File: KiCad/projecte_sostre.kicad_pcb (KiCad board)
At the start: 2 copper layers, 97.6 x 92.1 mm, 149 parts, among them J1 Conn_01x02, J10 DE9_Pins, J11 DE9_Pins, J2 Conn_01x05, J3 Conn_01x02, J4 Conn_01x02, J5 Conn_01x02, J6 Conn_01x02, J7 Screw_Terminal_01x02, J8 Screw_Terminal_01x02, J9 Screw_Terminal_01x02, SW1 SW_Push, SW2 SW_Push, SW3 SW_Push, SW4 SW_Push, SW5 SW_Push, SW6 SW_Push, U1 74AHCT1G125, U10 MCP2561-E-MF, U11 MAX3232, U12 A1101xLH, U13 A1101xLH, U14 L298P, U2 LM393, U3 LM393, U4 PIC24HJ128GP502, U5 LM1117DT-3.3, U6 LM2596T-5, U8 INA219AxD, U9 INA219AxD, Y1 Crystal

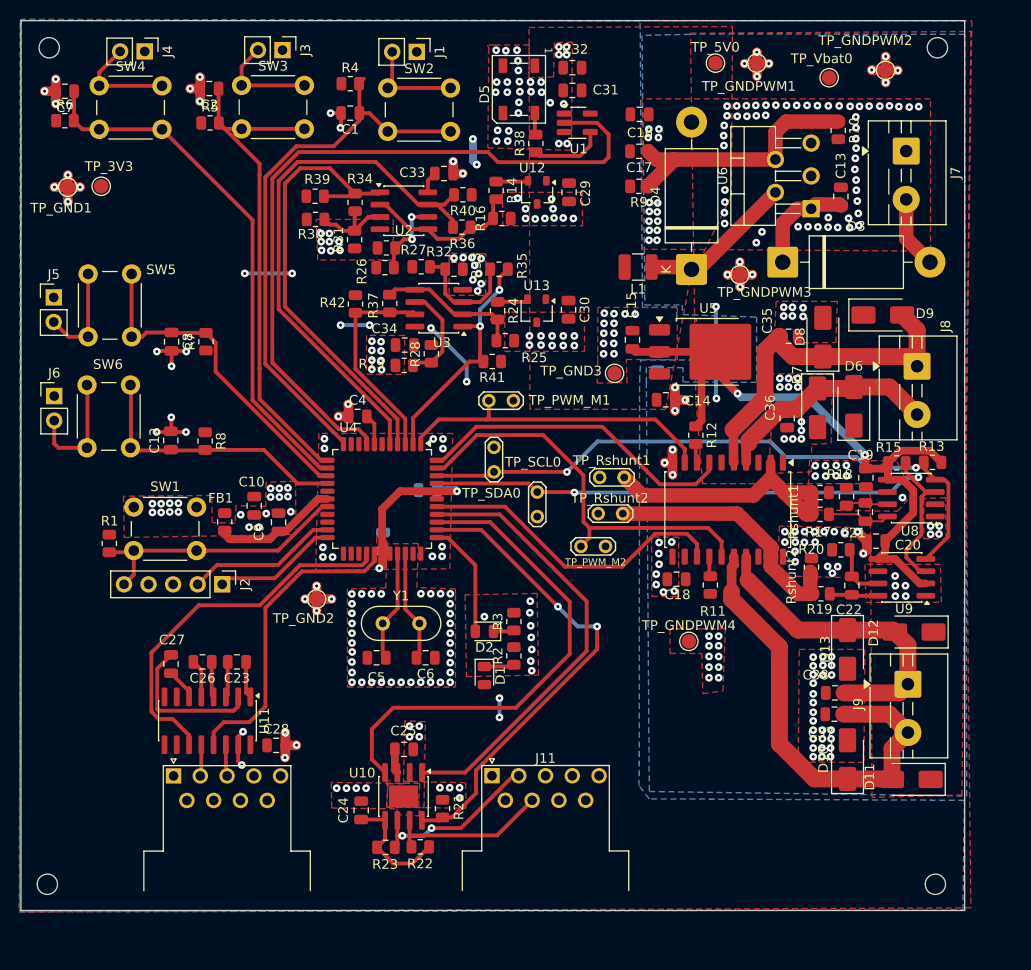
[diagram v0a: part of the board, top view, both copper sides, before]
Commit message: PCB casi acabada, despues de revisión de ayer 27/04 y cambio en componente CAN, que se vera reflejado en README y en DB
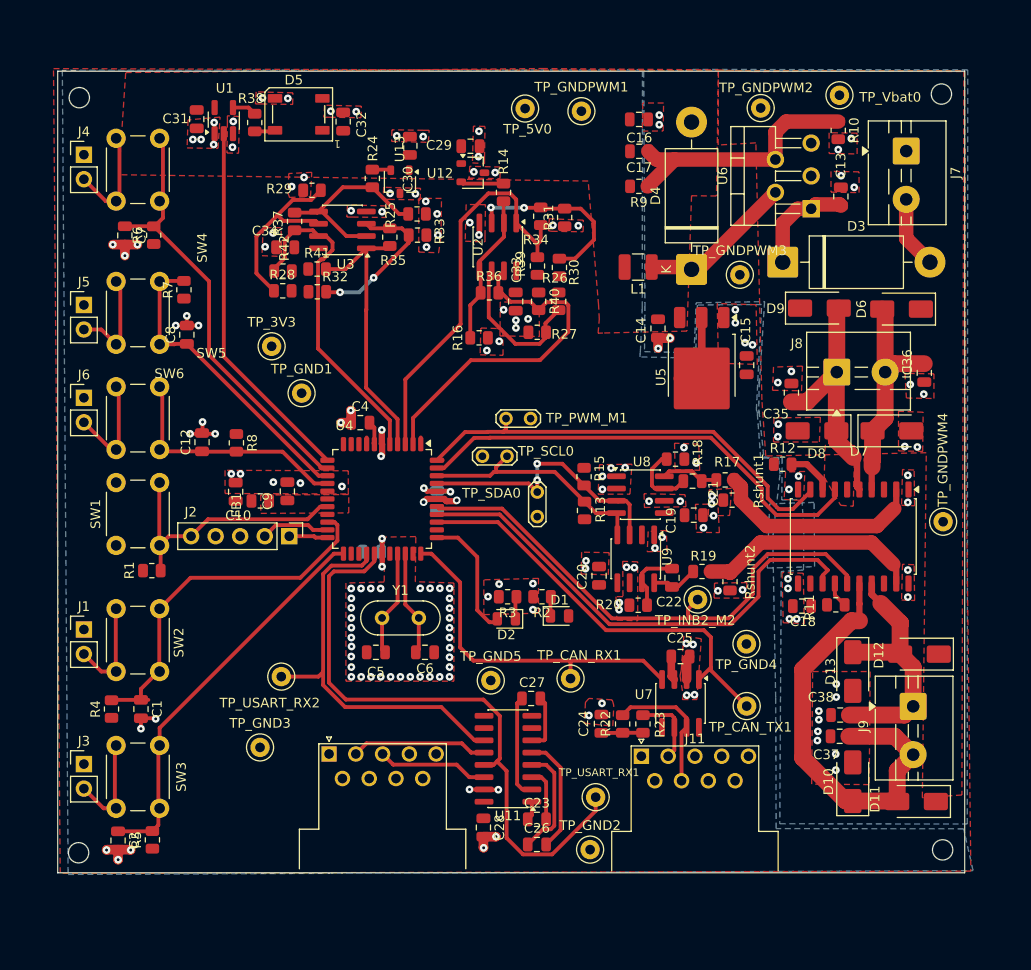
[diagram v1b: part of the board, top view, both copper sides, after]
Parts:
- removed R21: 10k, Resistor_SMD:R_0805_2012Metric
- removed R43: 0, Resistor_SMD:R_0805_2012Metric
- removed TP_PWM_M2, TP_Rshunt1, TP_Rshunt2: TestPoint_2Pole, TestPoint:TestPoint_2Pads_Pitch2.54mm_Drill0.8mm
- removed U10: MCP2561-E-MF, Package_SO:SOIC-8-1EP_3.9x4.9mm_P1.27mm_EP2.29x3mm
- added TP_CAN_RX1: TestPoint, TestPoint:TestPoint_Keystone_5000-5004_Miniature, F.Cu at (157.4, 123.7)
- added TP_CAN_TX1: TestPoint, TestPoint:TestPoint_Keystone_5000-5004_Miniature, F.Cu at (175.7, 126.5)
- added TP_GND4: TestPoint, TestPoint:TestPoint_Keystone_5000-5004_Miniature, F.Cu at (175.7, 120.1)
- added TP_GND5: TestPoint, TestPoint:TestPoint_Keystone_5000-5004_Miniature, F.Cu at (149.2, 123.9)
- added TP_INB2_M2: TestPoint, TestPoint:TestPoint_Keystone_5000-5004_Miniature, F.Cu at (170.6, 115.5)
- added TP_USART_RX1: TestPoint, TestPoint:TestPoint_Keystone_5000-5004_Miniature, F.Cu at (160.1, 135.9)
- added TP_USART_RX2: TestPoint, TestPoint:TestPoint_Keystone_5000-5004_Miniature, F.Cu at (127.5, 123.5)
- added U7: SN65HVD232, Package_SO:SOIC-8_3.9x4.9mm_P1.27mm, F.Cu at (168.8, 126.2)
- TP_3V3, TP_5V0, TP_GND1, TP_GND2, TP_GND3, TP_GNDPWM1, TP_GNDPWM2, TP_GNDPWM3, TP_GNDPWM4, TP_Vbat0: footprint TestPoint:TestPoint_Pad_D1.5mm -> TestPoint:TestPoint_Keystone_5000-5004_Miniature
- moved C2 78.4 mm to (110.6, 140.4), turned to -90 degrees
- moved J3 76.7 mm to (107.1, 132.5), turned to 0 degrees
- moved SW3 75.9 mm to (110.4, 137.1), turned to 90 degrees
- moved R5 74.4 mm to (114.2, 140.4), turned to 90 degrees
- moved R4 69.3 mm to (110.0, 126.8), turned to 90 degrees
- moved J1 69.0 mm to (107.1, 118.6), turned to 0 degrees
- moved SW2 66.6 mm to (110.4, 123.0), turned to 90 degrees
- moved C1 65.3 mm to (113.0, 126.8), turned to -90 degrees
- moved TP_GND3 53.3 mm to (125.3, 130.8)
- moved C26 39.4 mm to (154.0, 140.8), turned to 0 degrees
- moved C31 39.0 mm to (118.8, 65.8), turned to -90 degrees
- moved TP_GND2 38.4 mm to (159.5, 141.4)
- moved C27 37.4 mm to (153.4, 125.7), turned to 0 degrees
- moved U1 36.6 mm to (121.6, 66.0), turned to 90 degrees
- moved R13 36.4 mm to (158.9, 106.3), turned to 90 degrees
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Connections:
- net /Digital/SPLIT renamed /Digital/entre_R_par_diferencial_y_C
- C21 pad 1: /Analogica/IN+ -> /Analogica/IN+_M1
- C21 pad 2: /Analogica/IN- -> /Analogica/IN-_M1
- C22 pad 1: /Analogica/IN+ -> /Analogica/IN+_M2
- C22 pad 2: /Analogica/IN- -> /Analogica/IN-_M2
- R17 pad 1: /Analogica/IN+ -> /Analogica/IN+_M1
- R18 pad 2: /Analogica/IN- -> /Analogica/IN-_M1
- R19 pad 1: /Analogica/IN+ -> /Analogica/IN+_M2
- R20 pad 2: /Analogica/IN- -> /Analogica/IN-_M2
- U4 pad 1: INA2_M1 -> unconnected-(U4-RB9-Pad1)
- U4 pad 11: M1_go_Max -> unconnected-(U4-RB13-Pad11)
- U4 pad 12: M1_go_Min -> LED_RGB
- U4 pad 2: DOWN_LOW_M1_Pos_Min -> HIGH_UP_M1_Pos_Max
- U4 pad 20: unconnected-(U4-AN1/C12IN1-/CTCMP/RA1-Pad20) -> M1_go_Max
- U4 pad 23: unconnected-(U4-RB2-Pad23) -> M1_go_Min
- U4 pad 3: HIGH_UP_M1_Pos_Min -> DOWN_LOW_M1_Pos_Max
- U4 pad 33: unconnected-(U4-RB4-Pad33) -> CAN_RX
- U4 pad 35: STBY_Trans_CAN -> unconnected-(U4-RA9-Pad35)
- U4 pad 36: CAN_RX -> CAN_TX
- U4 pad 37: CAN_TX -> INB1_M2
- U4 pad 38: INB1_M2 -> INB2_M2
- U4 pad 4: DOWN_LOW_M1_Pos_Max -> DOWN_LOW_M1_Pos_Min
- U4 pad 43: INB2_M2 -> INA1_M1
- U4 pad 44: INA1_M1 -> INA2_M1
- U4 pad 5: HIGH_UP_M1_Pos_Max -> HIGH_UP_M1_Pos_Min
- U4 pad 8: LED_RGB -> unconnected-(U4-PGED2/RB10-Pad8)
- U8 pad 7: /Analogica/IN- -> /Analogica/IN-_M1
- U8 pad 8: /Analogica/IN+ -> /Analogica/IN+_M1
- U9 pad 7: /Analogica/IN- -> /Analogica/IN-_M2
- U9 pad 8: /Analogica/IN+ -> /Analogica/IN+_M2
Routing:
- net +3.3V: track 115.0 -> 25.8 mm, vias 14 -> 4
- net STBY_Trans_CAN: track 49.9 -> 0.00 mm, vias 2 -> 0
- net I2C_SCL: track 66.0 -> 24.9 mm, vias 2 -> 0
- net I2C_SDA: track 67.2 -> 28.2 mm
- net LED_RGB: track 76.8 -> 38.2 mm
- net USART_RX: track 32.0 -> 64.1 mm
- net GND: track 67.9 -> 36.1 mm, vias 384 -> 172
- net HIGH_UP_M1_Pos_Max: track 57.2 -> 36.2 mm
- net M1_go_Max: track 57.9 -> 38.1 mm
- net INB1_M2: track 32.7 -> 51.5 mm
- net CAN_RX: track 51.3 -> 36.2 mm
- net INA1_M1: track 33.5 -> 48.1 mm
- net INB2_M2: track 42.1 -> 55.8 mm
- net INA2_M1: track 33.5 -> 47.0 mm
- net /Microprocesador/AVDD: track 12.9 -> 0.00 mm
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- added copper zone on F.Cu, net /Microprocesador/AVDD
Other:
- board size 97.6 x 92.1 mm -> 93.8 x 82.9 mm

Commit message: Layout definitivo
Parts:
- removed C33: 100n, Capacitor_SMD:C_0805_2012Metric
- removed R24, R26, R28, R31, R33, R39, R40, R41, R42: 10k, Resistor_SMD:R_0805_2012Metric
- removed R25: 20k, Resistor_SMD:R_0805_2012Metric
- removed R27, R29, R30, R32: 22k, Resistor_SMD:R_0805_2012Metric
- removed R34, R35, R36, R37: 220k, Resistor_SMD:R_0805_2012Metric
- removed TP_PWM_M1, TP_SCL0, TP_SDA0: TestPoint_2Pole, TestPoint:TestPoint_2Pads_Pitch2.54mm_Drill0.8mm
- removed U2: LM393, Package_SO:SOIC-8_3.9x4.9mm_P1.27mm
- added GND10: TestPoint, TestPoint:TestPoint_Keystone_5000-5004_Miniature, F.Cu at (158.4, 95.2)
- added PWM_M1: TestPoint, TestPoint:TestPoint_Keystone_5000-5004_Miniature, F.Cu at (153.0, 97.3)
- added SCL0: TestPoint, TestPoint:TestPoint_Keystone_5000-5004_Miniature, F.Cu at (149.9, 100.7)
- added SDA0: TestPoint, TestPoint:TestPoint_Keystone_5000-5004_Miniature, F.Cu at (153.9, 104.5)
- R16: value 20k -> 10k
- moved RX2 25.0 mm to (137.2, 125.8)
- moved C34 24.3 mm to (150.4, 88.3), turned to 0 degrees
- moved TP_3V3 15.7 mm to (123.0, 74.0)
- moved GND1 15.6 mm to (123.0, 80.0)
- moved U3 14.6 mm to (145.9, 85.6), turned to -90 degrees
- moved TX2 13.8 mm to (140.6, 128.0)
- moved U13 13.7 mm to (151.9, 78.8), turned to 0 degrees
- moved R14 13.1 mm to (140.6, 81.9), turned to 0 degrees
- moved C30 13.0 mm to (151.6, 75.8), turned to 0 degrees
- moved C26 9.29 mm to (156.7, 131.9), turned to 90 degrees
- moved U12 8.84 mm to (142.6, 78.8)
- moved C29 8.63 mm to (142.5, 75.9)
- moved R16 8.20 mm to (153.1, 82.0)
- moved C15 7.68 mm to (169.6, 95.9), turned to 0 degrees
- moved C14 6.89 mm to (173.3, 86.7), turned to 180 degrees
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- renumbered TP_GND1 to GND1, TP_GNDPWM1 to GND2, TP_GNDPWM2 to GND3, TP_GND5 to GND4, TP_GND2 to GND5, TP_GND3 to GND6, TP_GNDPWM3 to GND7, TP_GNDPWM4 to GND8, TP_GND4 to GND9, TP_INB2_M2 to PWM_M2, TP_CAN_RX1 to RX1, TP_USART_RX1 to RX2, Rshunt1 to Rsht1, Rshunt2 to Rsht2, TP_CAN_TX1 to TX1, TP_USART_RX2 to TX2
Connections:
- J1 pad 2: /Microprocesador/Conn_SW_M1_Max -> M1_go_Max
- J3 pad 2: /Microprocesador/Conn_SW_M1_Min -> M1_go_Min
- J4 pad 2: /Microprocesador/Conn_SW_M2_Max -> M2_go_Max
- J5 pad 2: /Microprocesador/Conn_SW_M2_Min -> M2_go_Min
- J6 pad 2: /Microprocesador/Conn_SW_LED_ON/OFF -> ON/OFF_LED
- R14 pad 1: /Digital/SHall1_entre_Vout_y_Rdivisor -> +3.3V
- R14 pad 2: /Digital/VOUT_Hall1 -> /Digital/entre_sHall_R14
- R16 pad 1: GND -> +3.3V
- R16 pad 2: /Digital/VOUT_Hall1 -> /Digital/entre_sHall_R16
- SW2 pad 1: /Microprocesador/Conn_SW_M1_Max -> GND
- SW3 pad 1: /Microprocesador/Conn_SW_M1_Min -> GND
- SW4 pad 1: /Microprocesador/Conn_SW_M2_Max -> GND
- SW5 pad 1: /Microprocesador/Conn_SW_M2_Min -> GND
- SW6 pad 1: /Microprocesador/Conn_SW_LED_ON/OFF -> GND
- U12 pad 2: /Digital/SHall1_entre_Vout_y_Rdivisor -> /Digital/entre_sHall_R14
- U13 pad 2: /Digital/SHall2_entre_Vout_y_Rdivisor -> /Digital/entre_sHall_R16
- U3 pad 1: DOWN_LOW_M1_Pos_Min -> Pos_MAX
- U3 pad 2: /Digital/VOUT_Hall2 -> Pos_MAX
- U3 pad 3: /Digital/Vref_1V_Min -> /Digital/entre_sHall_R14
- U3 pad 5: /Digital/VOUT_Hall2 -> /Digital/entre_sHall_R16
- U3 pad 6: /Digital/Vref_2,2V_Min -> Pos_MIN
- U3 pad 7: HIGH_UP_M1_Pos_Min -> Pos_MIN
- U4 pad 2: HIGH_UP_M1_Pos_Max -> Pos_MIN
- U4 pad 3: DOWN_LOW_M1_Pos_Max -> unconnected-(U4-RC7-Pad3)
- U4 pad 4: DOWN_LOW_M1_Pos_Min -> unconnected-(U4-RC8-Pad4)
- U4 pad 5: HIGH_UP_M1_Pos_Min -> Pos_MAX
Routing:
- net DOWN_LOW_M1_Pos_Max: track 41.7 -> 0.00 mm
- net HIGH_UP_M1_Pos_Max: track 36.2 -> 0.00 mm
- net HIGH_UP_M1_Pos_Min: track 34.1 -> 0.00 mm
- net GND: track 36.1 -> 70.1 mm, vias 172 -> 160
- net DOWN_LOW_M1_Pos_Min: track 29.2 -> 0.00 mm
- net USART_RX: track 64.1 -> 42.6 mm
- net Pos_MAX: track 0.00 -> 20.8 mm
- net /Digital/VOUT_Hall2: track 20.0 -> 0.00 mm
- net /Digital/Vref_2,2V_Min: track 20.0 -> 0.00 mm
- net /Digital/Vref_1V_Max: track 19.2 -> 0.00 mm, vias 2 -> 0
- net /Digital/Vref_1V_Min: track 16.3 -> 0.00 mm, vias 2 -> 0
- net /Digital/VOUT_Hall1: track 15.7 -> 0.00 mm
- net /Digital/Vref_2,2V_Max: track 15.6 -> 0.00 mm
- net Pos_MIN: track 0.00 -> 14.3 mm
- net /Digital/entre_sHall_R16: track 0.00 -> 14.3 mm
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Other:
- board text added: "CAN"
- board text added: "GND reducir tamaño, todo tamaño de pista igual o menor que tamaño de pad, que no sobresalga"
- board text added: "UART"

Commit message: layout final
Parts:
- moved PWM_M1 2.05 mm to (153.1, 95.2)
- moved GND3 1.33 mm to (177.1, 63.3)
- moved SCL0 0.55 mm to (150.3, 101.0)
- moved GND2 0.27 mm to (154.8, 65.6)
- moved GND8 0.25 mm to (195.8, 107.4)
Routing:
- net INA2_M1: track 46.2 -> 48.3 mm
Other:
- board text removed: "GND reducir tamaño, todo tamaño de pista igual o menor que tamaño de pad, que no sobresalga"
